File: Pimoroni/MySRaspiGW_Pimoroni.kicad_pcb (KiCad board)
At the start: 2 copper layers, 11.5 x 16.2 mm, 5 parts, among them P1 CONN_02X04, U1 NRF24L01

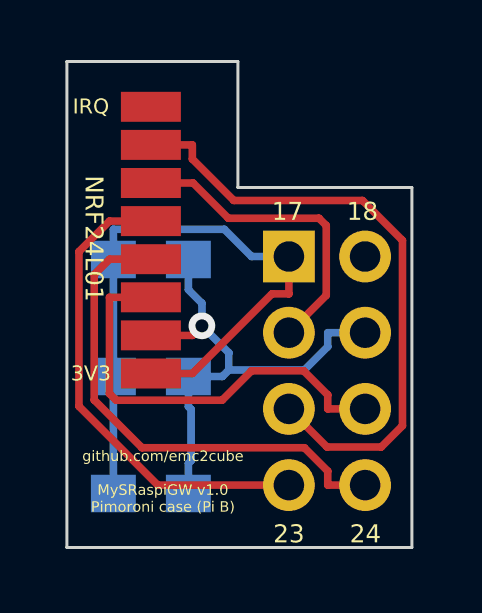
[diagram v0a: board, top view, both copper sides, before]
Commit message: v1.1 IRQ support
Added IRQ support on pin 18
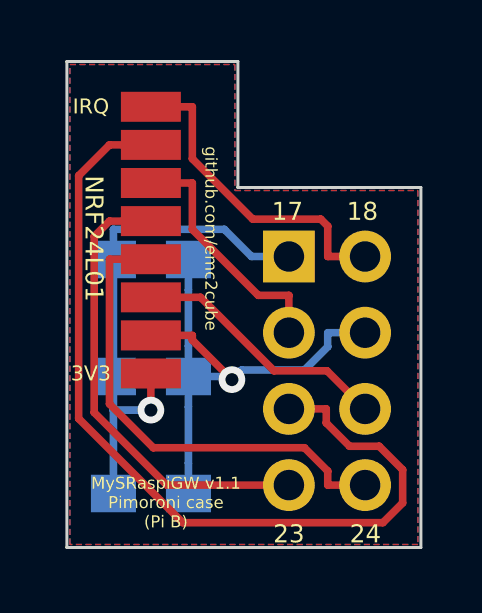
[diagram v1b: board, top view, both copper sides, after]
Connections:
- P1 pad 2: Net-(P1-Pad2) -> IRQ
- U1 pad 8: Net-(U1-Pad8) -> IRQ
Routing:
- net IRQ: track 0.00 -> 10.8 mm
- net MISO: track 20.8 -> 29.5 mm
- net CE: track 14.4 -> 8.68 mm
- net +3V3: track 22.0 -> 17.5 mm, vias 0 -> 1
- net MOSI: track 10.5 -> 8.30 mm
- net GND: track 16.8 -> 18.1 mm
- net CSN: track 16.8 -> 16.1 mm
- net SCK: track 16.1 -> 15.5 mm
- added copper zone on B.Cu, net GND
- added copper zone on F.Cu, net GND
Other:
- board size 11.5 x 16.2 mm -> 11.8 x 16.2 mm
- board text added: "MySRaspiGW v1.1 Pimoroni case (Pi B)"
- board text added: "github.com/emc2cube"
- board text removed: "github.com/emc2cube MySRaspiGW v1.0 Pimoroni case (Pi B)"
